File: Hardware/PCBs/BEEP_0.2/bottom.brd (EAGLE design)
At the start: 85 x 73 mm, 64 parts, among them IC1 74HCT00D, IC2 TCS32X0, IC3 TCS32X0, IC4 TCS32X0, Q1 DMN2075U, Q2 IRLML2244, Q5 IRLML2244, Q6 IRLML2244, Q8 IRLML2244, U1 LM239AMDREP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

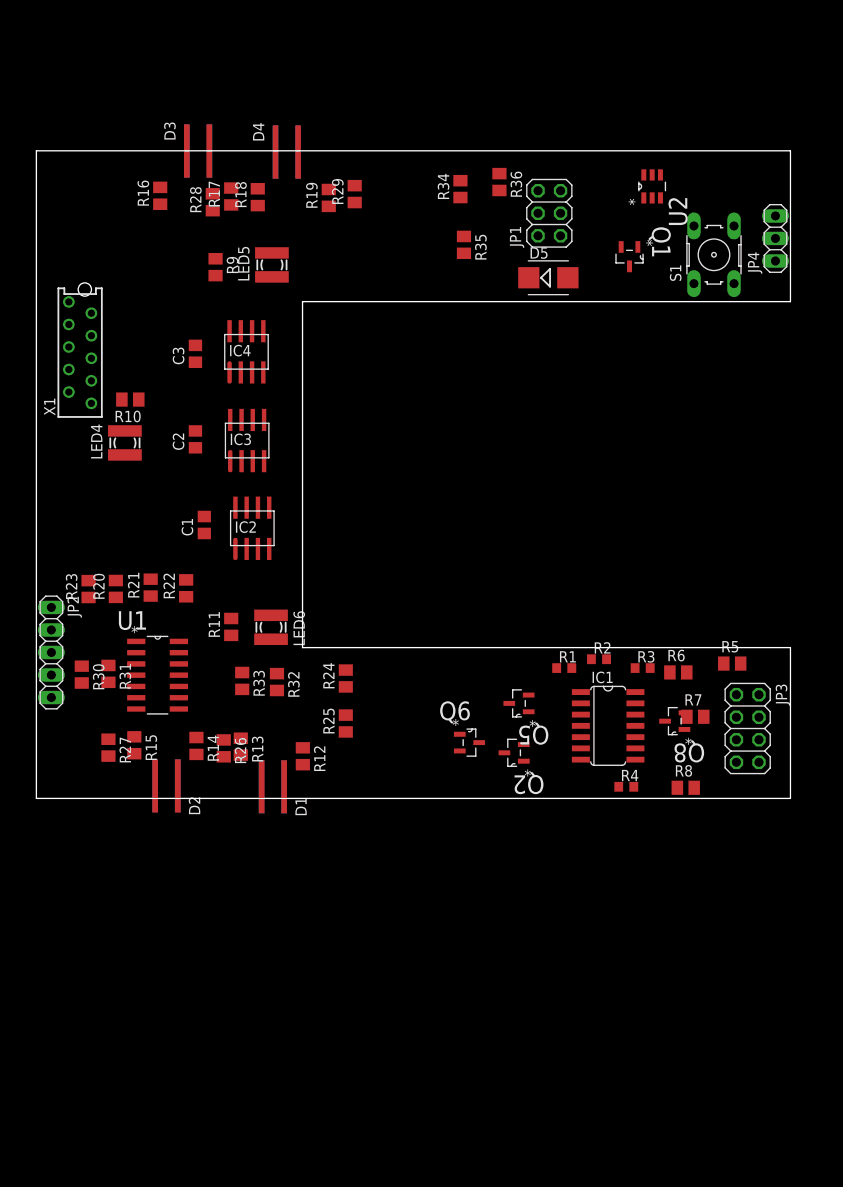
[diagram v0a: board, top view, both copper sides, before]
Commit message: started routing of the bottom pcb
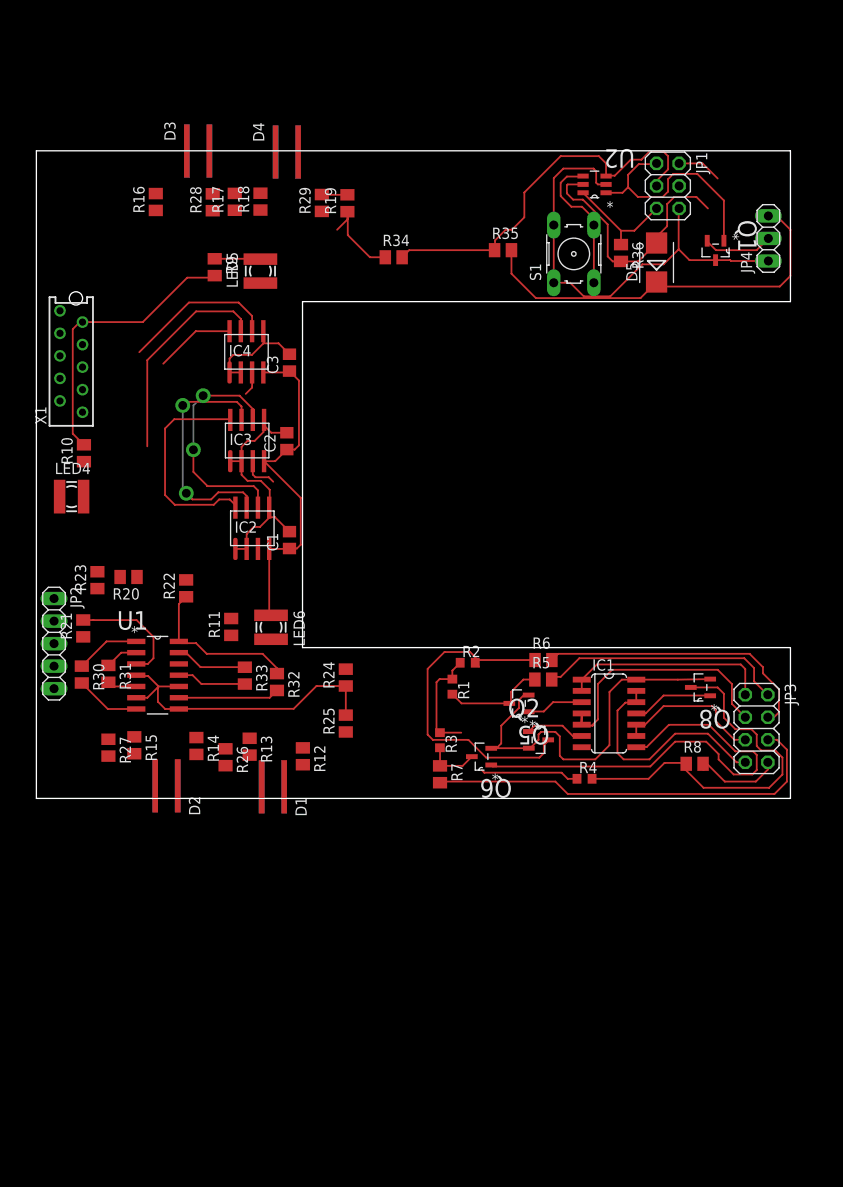
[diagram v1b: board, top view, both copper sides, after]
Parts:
- moved R7 29.5 mm to (45.5, 2.72), turned to 270 degrees
- moved R3 24.3 mm to (45.5, 6.56), turned to 270 degrees
- moved R5 21.4 mm to (57.1, 13.4)
- moved R36 15.9 mm to (65.9, 61.5)
- moved S1 15.8 mm to (60.6, 61.4)
- moved R6 15.3 mm to (57.2, 15.6)
- moved R2 14.8 mm to (48.6, 15.3)
- moved JP1 13.7 mm to (71.2, 69.0), turned to 270 degrees
- moved R1 12.8 mm to (46.9, 12.6), turned to 270 degrees
- moved D5 12.3 mm to (69.9, 60.4), turned to 90 degrees
- moved R34 10.7 mm to (40.3, 61.0), turned to 0 degrees
- moved C3 10.6 mm to (28.5, 49.1)
- moved C2 10.3 mm to (28.2, 40.3)
- moved C1 9.75 mm to (28.5, 29.1)
- moved Q1 9.73 mm to (76.6, 61.8)
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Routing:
- net GND: track 0.00 -> 72.9 mm
- net +3V3: track 0.00 -> 54.0 mm
- net BATT_GND: track 0.00 -> 51.8 mm
- net COLOR_DIODE_1: track 0.00 -> 51.8 mm, vias 0 -> 2
- net N$4: track 0.00 -> 51.0 mm
- net PWM_OUT3: track 0.00 -> 46.5 mm
- net +7V: track 0.00 -> 45.0 mm
- net COLOR_FREQ_OUT: track 0.00 -> 44.0 mm, vias 0 -> 2
- net TPICLK: track 0.00 -> 44.0 mm
- net +5V: track 0.00 -> 43.7 mm
- net N$13: track 0.00 -> 42.9 mm
- net N$15: track 0.00 -> 38.0 mm
- net U_REF: track 0.00 -> 35.9 mm
- net TINY_VCC: track 0.00 -> 34.4 mm
- net COLOR_DIODE_2: track 0.00 -> 33.6 mm
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
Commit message: continue work on bottom pcb
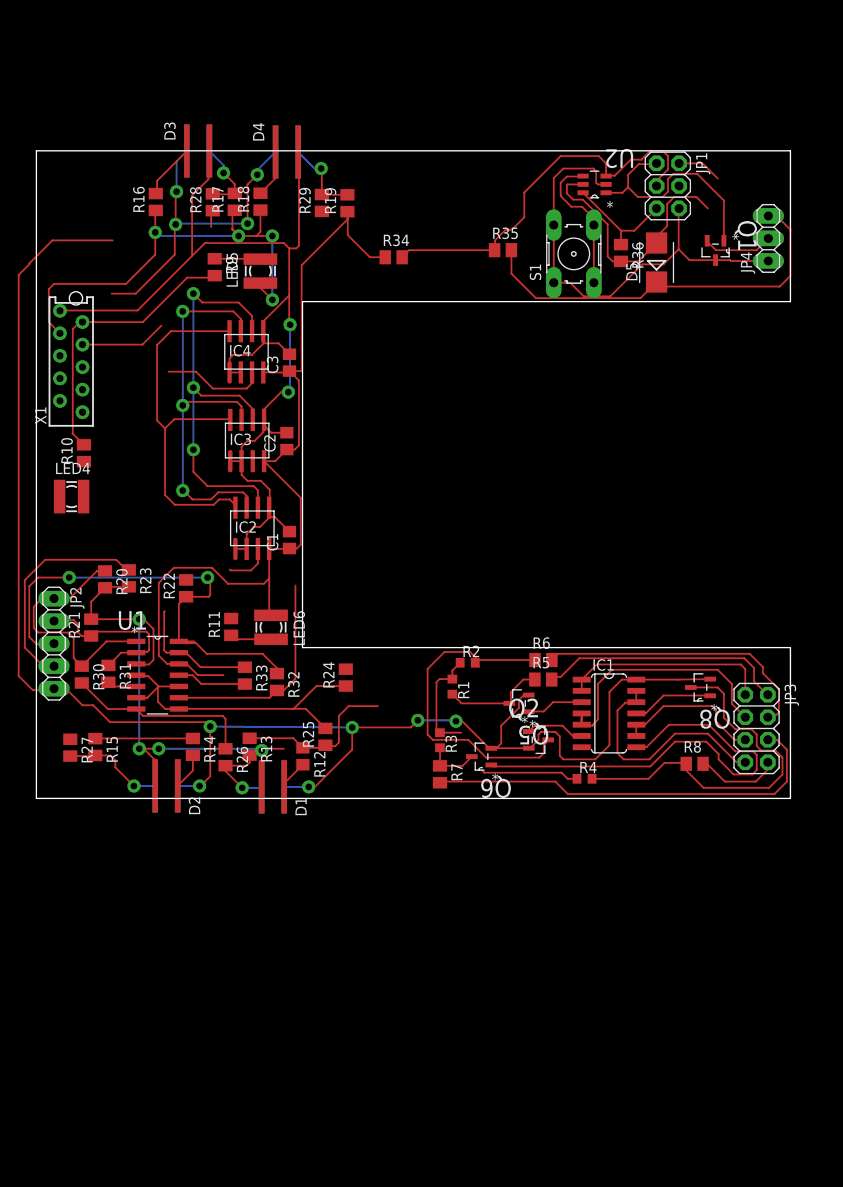
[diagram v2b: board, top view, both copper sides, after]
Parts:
- R12: device rcl:M0805 -> rcl:R0805
- moved R15 4.40 mm to (6.64, 5.79)
- moved R27 4.30 mm to (3.82, 5.72)
- moved R23 3.55 mm to (10.4, 24.8), turned to 270 degrees
- moved R25 2.75 mm to (32.6, 6.94)
- moved R20 2.66 mm to (7.74, 24.7), turned to 270 degrees
- moved R21 0.91 mm to (6.18, 19.3)
- moved R14 0.41 mm to (17.6, 5.81)
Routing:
- net +5V: track 43.7 -> 220.0 mm, vias 0 -> 10
- net GND: track 72.9 -> 206.8 mm, vias 0 -> 4
- net +3V3: track 54.0 -> 181.6 mm, vias 0 -> 6
- net ENC_R1: track 18.3 -> 54.3 mm, vias 0 -> 2
- net ENC_R2: track 8.12 -> 39.2 mm
- net ENC_L1: track 7.30 -> 27.9 mm
- net ENC_L2: track 3.74 -> 19.4 mm
- net N$47: track 11.4 -> 26.5 mm
- net COLOR_FREQ_OUT: track 44.0 -> 58.3 mm, vias 2 -> 3
- net N$44: track 7.35 -> 21.3 mm
- net ENC_L2_RAW: track 0.00 -> 11.5 mm, vias 0 -> 1
- net ENC_R1_RAW: track 0.00 -> 9.66 mm, vias 0 -> 1
- net COLOR_DIODE_2: track 33.6 -> 43.2 mm
- net ENC_L1_RAW: track 0.00 -> 9.21 mm, vias 0 -> 1
- net COLOR_SENSOR_3: track 2.71 -> 11.7 mm
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
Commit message: continue work on bottom pcb
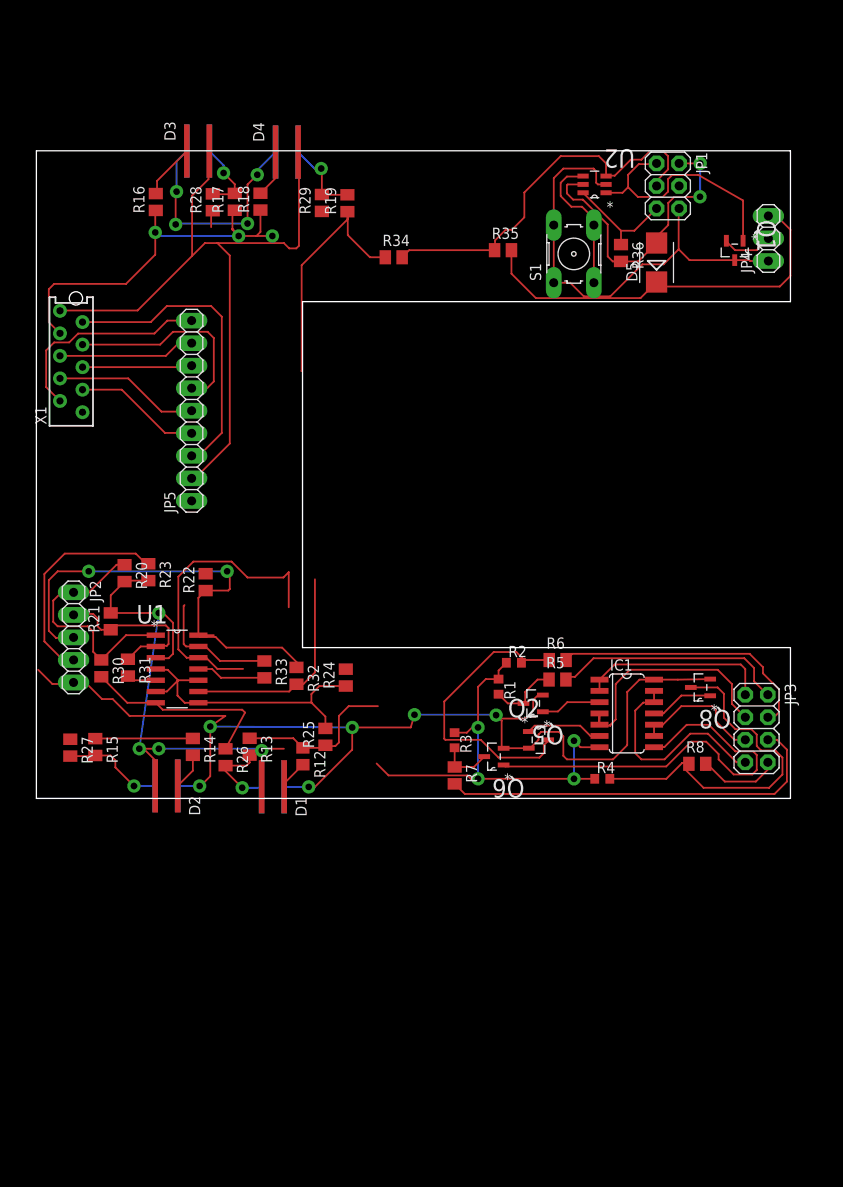
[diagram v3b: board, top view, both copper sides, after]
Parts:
- removed C1, C2, C3: 100n, rcl:C0805
- removed IC2, IC3, IC4: TCS32X0, BEEP:TCS32X0
- removed LED4, LED5, LED6: NFSG036BT, led:NFSG036BT
- removed R10, R11, R9: (no value), rcl:M0805
- added JP5: (no value), pinhead:1X09
- moved R1 5.21 mm to (52.1, 12.6)
- moved R2 5.21 mm to (53.8, 15.3)
- moved U1 2.31 mm to (18.3, 10.8)
- moved R31 2.31 mm to (10.3, 14.7)
- moved R21 2.31 mm to (8.38, 20.0)
- moved JP2 2.31 mm to (4.19, 18.1)
- moved R30 2.31 mm to (7.32, 14.7)
- moved R32 2.31 mm to (29.3, 13.8)
- moved R20 2.31 mm to (9.94, 25.4)
- moved R22 2.31 mm to (19.1, 24.4)
- moved R23 2.31 mm to (12.6, 25.5)
- moved R33 2.31 mm to (25.7, 14.5)
- moved Q1 2.16 mm to (78.7, 61.8)
- moved IC1 2.00 mm to (66.5, 9.58)
- moved R4 2.00 mm to (63.8, 2.21)
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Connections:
- removed net N$17: LED5.A, R9.1
- removed net N$18: LED4.A, R10.1
- removed net N$19: LED6.A, R11.1
- net +3V3: now also JP5.2; no longer C1.2, C2.2, C3.2, IC2.S0, IC2.S1, IC2.VDD, IC3.S0, IC3.S1, IC3.VDD, IC4.S0, IC4.S1, IC4.VDD
- net COLOR_DIODE_1: now also JP5.5; no longer IC2.S2, IC3.S2, IC4.S2
- net COLOR_DIODE_2: now also JP5.4; no longer IC2.S3, IC3.S3, IC4.S3
- net COLOR_FREQ_OUT: now also JP5.6; no longer IC2.OUT, IC3.OUT, IC4.OUT
- net COLOR_SENSOR_1: now also JP5.9; no longer IC2.NOE
- net COLOR_SENSOR_2: now also JP5.8; no longer IC3.NOE
- net COLOR_SENSOR_3: now also JP5.7; no longer IC4.NOE
- net COLOR_SENSOR_PWM_LED: now also JP5.3; no longer R10.2, R11.2, R9.2
- net GND: now also JP5.1; no longer C1.1, C2.1, C3.1, IC2.GND, IC3.GND, IC4.GND, LED4.C, LED5.C, LED6.C
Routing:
- net +5V: track 220.0 -> 153.8 mm
- net +3V3: track 181.6 -> 144.8 mm, vias 6 -> 4
- net COLOR_FREQ_OUT: track 58.3 -> 23.4 mm, vias 3 -> 0
- net COLOR_DIODE_1: track 46.7 -> 16.4 mm, vias 3 -> 0
- net COLOR_DIODE_2: track 43.2 -> 14.3 mm
- net COLOR_SENSOR_1: track 5.19 -> 24.1 mm
- net GND: track 206.8 -> 188.2 mm, vias 4 -> 7
- net COLOR_SENSOR_2: track 0.00 -> 15.4 mm
- net N$17: track 5.17 -> 0.00 mm
- net N$19: track 4.67 -> 0.00 mm
- net N$15: track 38.0 -> 33.4 mm
- net N$3: track 11.5 -> 7.88 mm
- net N$4: track 51.0 -> 47.6 mm
- net U_REF: track 37.1 -> 34.2 mm
- net COLOR_SENSOR_PWM_LED: track 32.1 -> 34.8 mm
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
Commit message: continue work on bottom pcbs
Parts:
- added U$1, U$2: (no value), holes:3,0
- JP4: device pinhead:1X03 -> pinhead:1X04
- moved X1 78.3 mm to (82.0, 55.1)
- moved JP3 74.7 mm to (6.48, 8.03)
- moved JP4 69.4 mm to (13.2, 61.4), turned to 270 degrees
- moved R30 65.6 mm to (72.9, 15.0), flipped to the bottom
- moved R21 64.3 mm to (72.6, 22.1), flipped to the bottom
- moved Q8 62.6 mm to (12.3, 12.7), flipped to the bottom
- moved R8 62.5 mm to (12.0, 3.04), flipped to the bottom
- moved Q1 61.6 mm to (17.1, 63.3), flipped to the bottom
- moved R31 60.6 mm to (70.9, 15.0), flipped to the bottom
- moved R20 60.5 mm to (70.4, 24.0), flipped to the bottom
- moved R15 56.6 mm to (63.3, 6.78), flipped to the bottom
- moved R23 55.7 mm to (68.3, 24.0), flipped to the bottom
- moved R27 55.6 mm to (59.4, 5.14), flipped to the bottom, turned to 0 degrees
- moved JP2 55.0 mm to (58.3, 28.0), turned to 90 degrees
- moved JP5 53.5 mm to (70.8, 38.7), turned to 270 degrees
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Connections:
- net +7V: now also JP4.4
- net BATT_GND: now also JP4.2; no longer JP4.1
- net PWM_IN1: now also JP3.2; no longer JP3.1
- net PWM_IN2: now also JP3.4; no longer JP3.3
- net PWM_IN3: now also JP3.6; no longer JP3.5
- net PWM_IN4: now also JP3.8; no longer JP3.7
- net PWM_OUT1: now also JP3.1; no longer JP3.2
- net PWM_OUT2: now also JP3.3; no longer JP3.4
- net PWM_OUT3: now also JP3.5; no longer JP3.6
- net PWM_OUT4: now also JP3.7; no longer JP3.8
- net SWITCHED_GND: now also JP4.1; no longer JP4.2
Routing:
- net N$49: track 7.85 -> 69.1 mm, vias 0 -> 2
- net +5V: track 153.8 -> 103.0 mm, vias 10 -> 4
- net COLOR_DIODE_2: track 14.3 -> 54.5 mm
- net COLOR_DIODE_1: track 16.4 -> 48.3 mm
- net ENC_R1: track 54.3 -> 24.8 mm, vias 2 -> 0
- net COLOR_SENSOR_3: track 12.4 -> 41.0 mm
- net +3V3: track 144.8 -> 167.8 mm, vias 4 -> 6
- net +7V: track 45.0 -> 22.6 mm
- net PWM_OUT3: track 44.7 -> 24.2 mm
- net ENC_L1_RAW: track 9.21 -> 26.7 mm
- net ENC_R1_RAW: track 9.66 -> 27.1 mm, vias 1 -> 3
- net N$47: track 26.5 -> 9.64 mm
- net N$14: track 5.98 -> 21.9 mm
- net N$45: track 3.33 -> 19.2 mm
- net COLOR_SENSOR_2: track 15.4 -> 31.2 mm
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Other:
- outline, holes or cut-outs redrawn

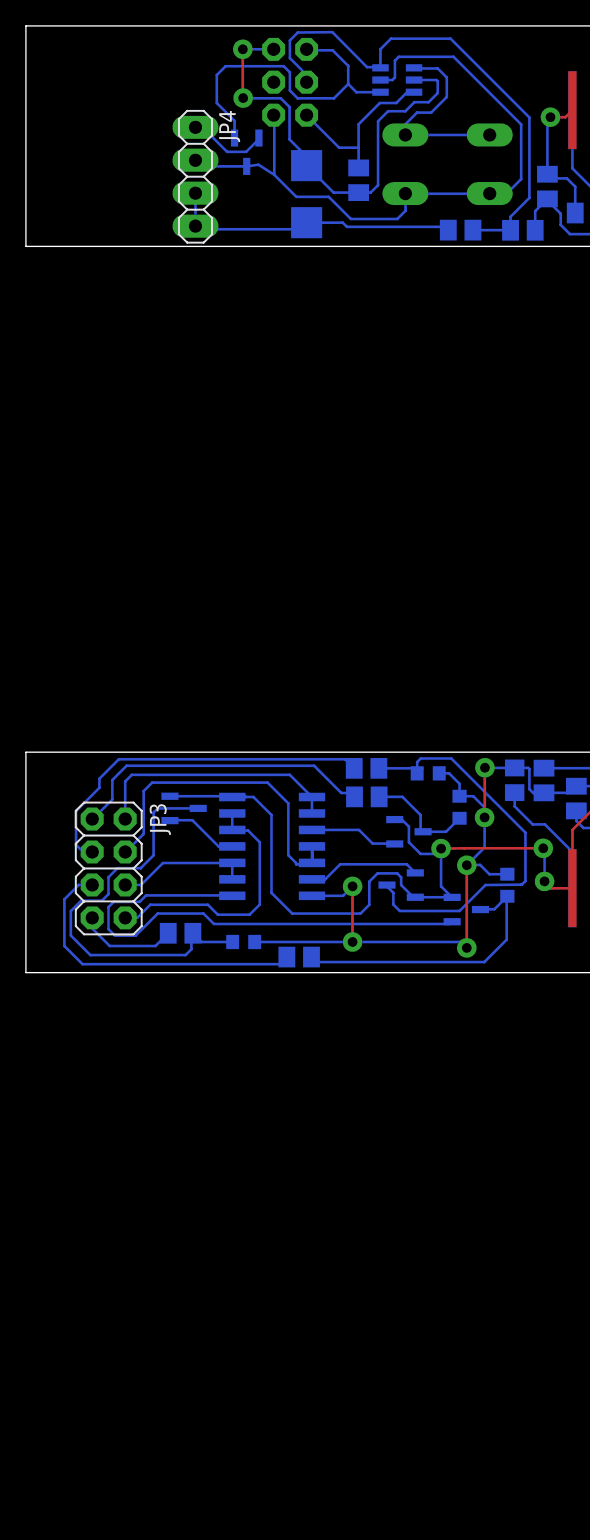
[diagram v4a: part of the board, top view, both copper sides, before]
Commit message: continue work on bottom pcb
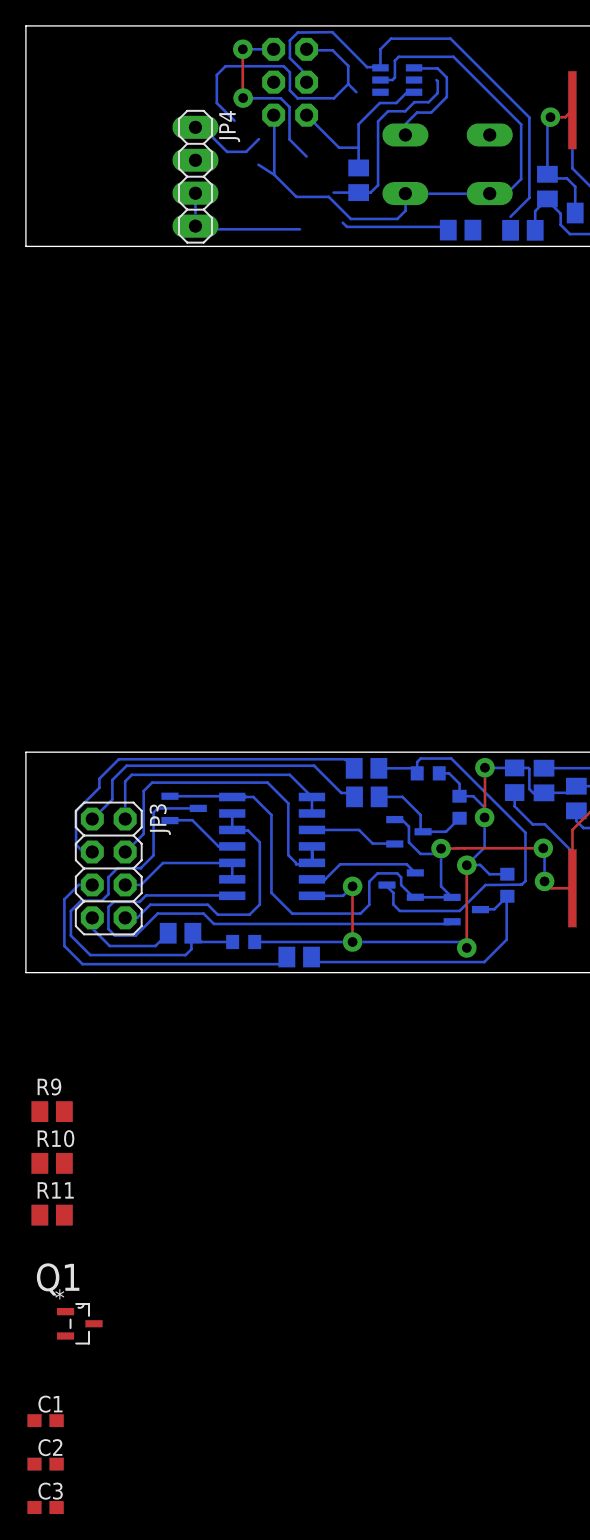
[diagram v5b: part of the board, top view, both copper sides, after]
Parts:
- removed D5: (no value), diode:SMB
- added C1, C2, C3: (no value), rcl:C0603
- added R10: 100k, rcl:M0805
- added R11: 1M, rcl:M0805
- added R9: 10k, rcl:M0805
- moved Q1 91.3 mm to (4.24, -27.1), flipped to the top, turned to 0 degrees
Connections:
- removed net N$6: S1.3, S1.4, U2.4
- new net PB0/TPIDATA: R9.1, U2.1
- new net PB1/TPICLK: Q1.G, R11.2, S1.1, S1.2, U2.3
- new net PB2/SOFT_OFF: R10.1, R9.2, S1.3, S1.4, U2.4
- net +3V3: now also C1.1, R10.2, R36.2, U2.5
- net +7V: no longer D5.C
- net BATT_GND: now also Q1.S, R11.1; no longer Q1.D, S1.1, S1.2, U2.2
- net GND: now also C1.2, U2.2
- net RESET: now also R34.2, R35.1
- net SWITCHED_GND: now also Q1.D; no longer Q1.S
- net TINY_VCC: no longer D5.A, R36.2, U2.5
- net TPICLK: no longer R34.2, R35.1, U2.3
- net TPIDATA: no longer Q1.G, U2.1
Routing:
- net TPICLK: track 40.1 -> 12.1 mm
- net BATT_GND: track 52.4 -> 26.3 mm
- net PB1/TPICLK: track 0.00 -> 24.0 mm
- net GND: track 178.1 -> 199.8 mm
- net TINY_VCC: track 34.9 -> 14.4 mm
- net N$6: track 15.7 -> 0.00 mm
- net +3V3: track 167.8 -> 182.9 mm
- net PB2/SOFT_OFF: track 0.00 -> 8.40 mm
- net +7V: track 22.6 -> 19.1 mm
- net TPIDATA: track 26.0 -> 22.8 mm
